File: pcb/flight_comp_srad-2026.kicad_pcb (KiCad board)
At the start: 2 copper layers, 70 x 40 mm, 41 parts, among them J1 503398-1892, J3 USB_B_Micro, U1 IIM-20670, U2 NCP1117-3.3_SOT223, U3 RP2040, U4 ADXL375BCCZ-RL7, U5 MAX-M10M-00B, U6 W25Q128JVS, U7 XBP9B-DMSTB002, Y1 ABM8-272-T3

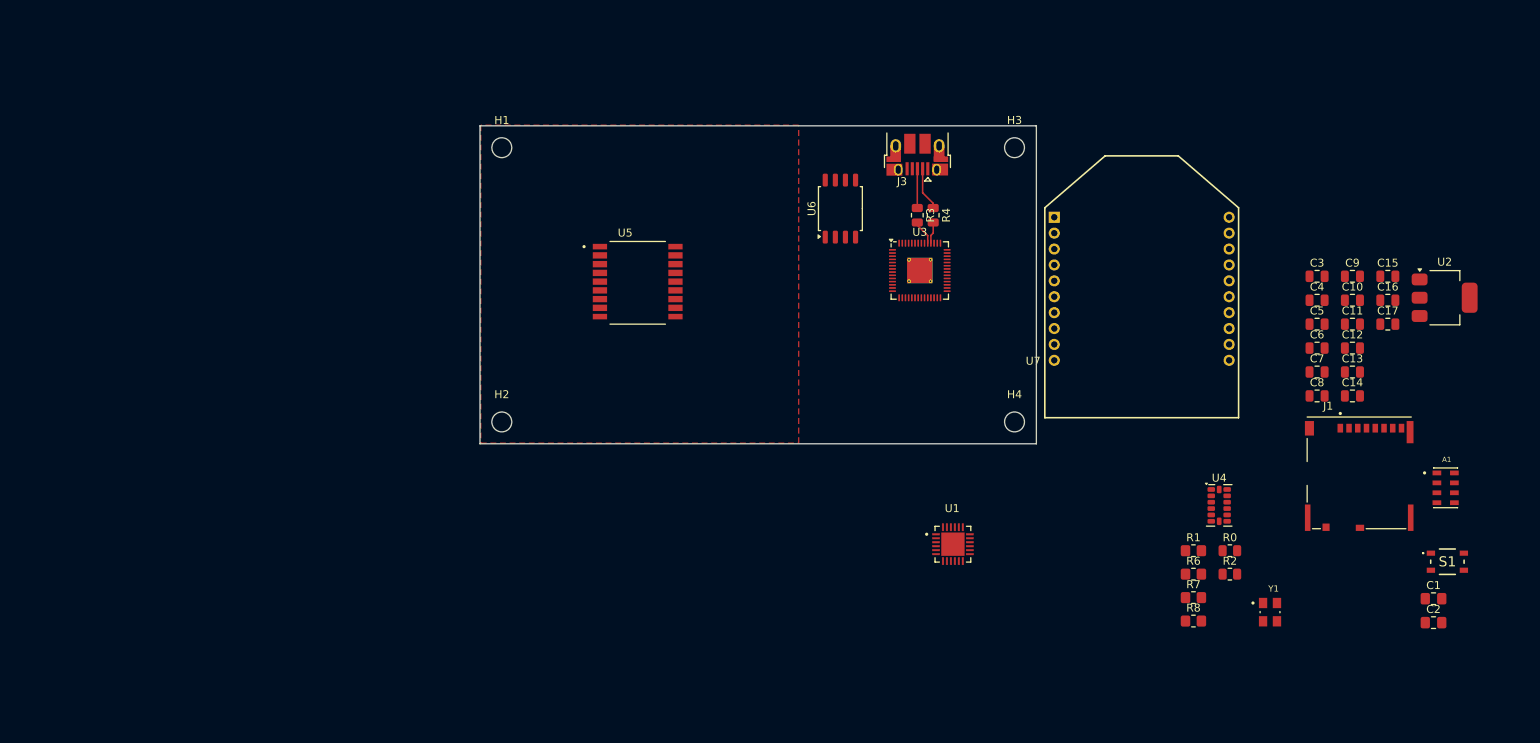
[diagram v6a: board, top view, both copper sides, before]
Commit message: RP2040 listo, faltan sensores y comms
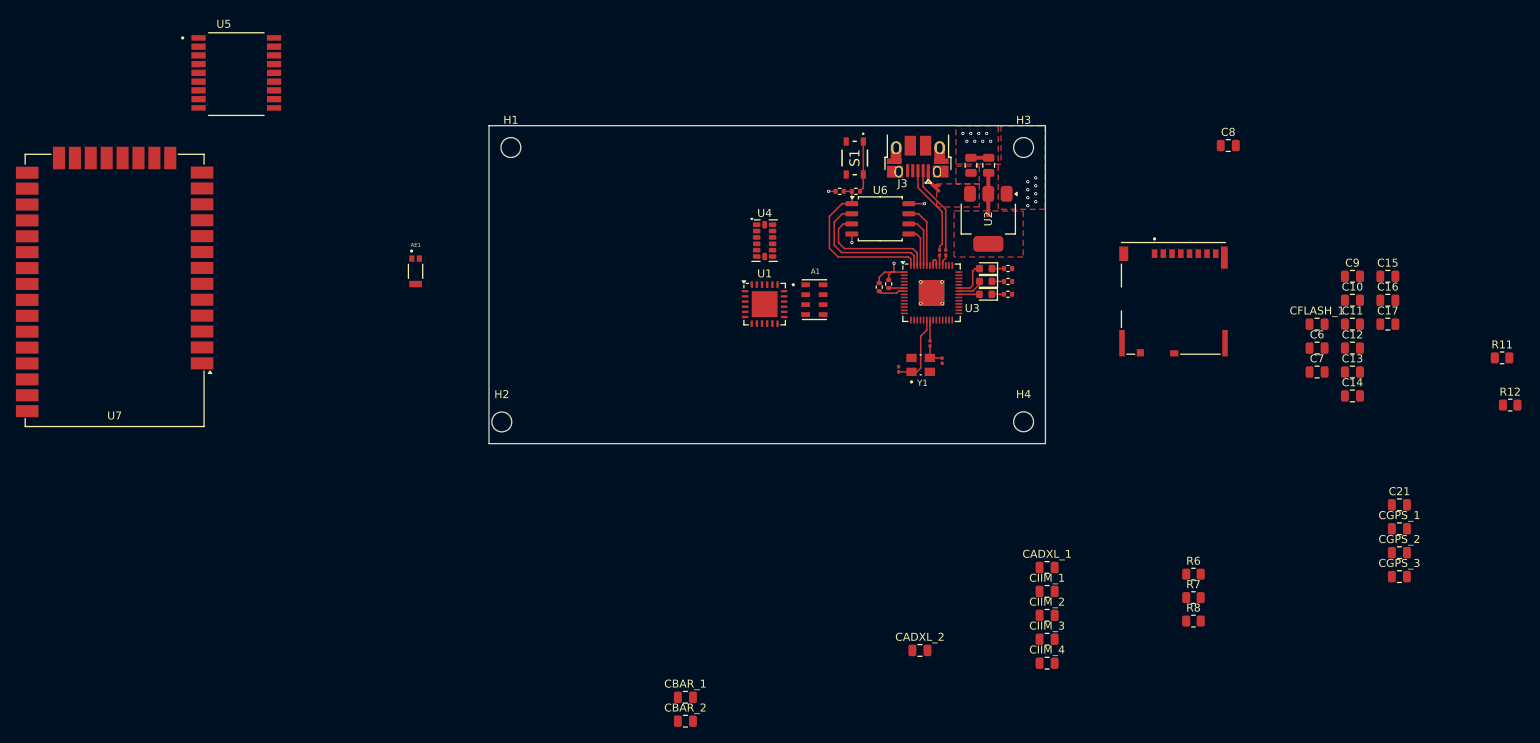
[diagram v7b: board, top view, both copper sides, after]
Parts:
- added AE1: W3011, W3011:XDCR_W3011, F.Cu at (141.9, 78.8)
- added C21: C, Capacitor_SMD:C_0805_2012Metric, F.Cu at (265.7, 108.2)
- added CADXL_1: 100n, Capacitor_SMD:C_0805_2012Metric, F.Cu at (221.3, 116.1)
- added CADXL_2: 1u, Capacitor_SMD:C_0805_2012Metric, F.Cu at (205.3, 126.5)
- added CBAR_1: 100n, Capacitor_SMD:C_0805_2012Metric, F.Cu at (175.8, 132.4)
- added CBAR_2: 100n, Capacitor_SMD:C_0805_2012Metric, F.Cu at (175.8, 135.4)
- added CGPS_1: 100n, Capacitor_SMD:C_0805_2012Metric, F.Cu at (265.7, 111.2)
- added CGPS_2: 100n, Capacitor_SMD:C_0805_2012Metric, F.Cu at (265.7, 114.2)
- added CGPS_3: 100n, Capacitor_SMD:C_0805_2012Metric, F.Cu at (265.7, 117.2)
- added CIIM_1: 100n, Capacitor_SMD:C_0805_2012Metric, F.Cu at (221.3, 119.1)
- added CIIM_2: 100n, Capacitor_SMD:C_0805_2012Metric, F.Cu at (221.3, 122.1)
- added CIIM_3: 100n, Capacitor_SMD:C_0805_2012Metric, F.Cu at (221.3, 125.1)
- added CIIM_4: 100n, Capacitor_SMD:C_0805_2012Metric, F.Cu at (221.3, 128.1)
- added D1: LED, LED_SMD:LED_0603_1608Metric, F.Cu at (213.6, 78.5)
- added D2: LED, LED_SMD:LED_0603_1608Metric, F.Cu at (213.6, 80.1)
- added D3: LED, LED_SMD:LED_0603_1608Metric, F.Cu at (213.6, 81.7)
- added R11: R, Resistor_SMD:R_0805_2012Metric, F.Cu at (278.6, 89.7)
- added R12: R, Resistor_SMD:R_0805_2012Metric, F.Cu at (279.6, 95.6)
- added RI2C_1: 10k, Resistor_SMD:R_0402_1005Metric, F.Cu at (200.2, 80.8)
- added RI2C_2: 10k, Resistor_SMD:R_0402_1005Metric, F.Cu at (201.4, 80.4)
- added RL_1: 1k, Resistor_SMD:R_0402_1005Metric, F.Cu at (216.4, 78.5)
- added RL_2: 1k, Resistor_SMD:R_0402_1005Metric, F.Cu at (216.4, 80.1)
- added RL_3: 1k, Resistor_SMD:R_0402_1005Metric, F.Cu at (216.4, 81.7)
- CX_1: renamed from C1; footprint TCLib:C_0805 -> Capacitor_SMD:C_0201_0603Metric
- CX_2: renamed from C2; footprint TCLib:C_0805 -> Capacitor_SMD:C_0201_0603Metric
- R3, R4: footprint Resistor_SMD:R_0805_2012Metric -> Capacitor_SMD:C_0201_0603Metric
- R6, R7, R8: footprint Resistor_SMD:R_0805_2012Metric_Pad1.20x1.40mm_HandSolder -> Resistor_SMD:R_0805_2012Metric
- RFLASH_1: renamed from R0; footprint Resistor_SMD:R_0805_2012Metric -> Resistor_SMD:R_0402_1005Metric
- RFLASH_2: renamed from R2; footprint Resistor_SMD:R_0805_2012Metric -> Resistor_SMD:R_0402_1005Metric
- RX_1: renamed from R1; footprint Resistor_SMD:R_0805_2012Metric_Pad1.20x1.40mm_HandSolder -> Resistor_SMD:R_0201_0603Metric
- U1: footprint IIM_20670:QFN50P450X450X115-25N -> Package_DFN_QFN:QFN-24-1EP_5x5mm_P0.65mm_EP3.25x3.25mm
- U7: footprint XBEEPRO:XBEEPRO -> RF_Module:Digi_XBee_SMT
- moved U7 129.2 mm to (104.0, 80.5), turned to 180 degrees
- moved S1 90.2 mm to (197.2, 64.5), turned to -90 degrees
- moved A1 82.9 mm to (192.1, 82.4)
- moved CX_1 73.2 mm to (202.7, 91.1), turned to -90 degrees
- moved CX_2 70.1 mm to (208.1, 90.0), turned to 90 degrees
- moved RFLASH_2 67.3 mm to (197.3, 68.7)
- moved RFLASH_1 66.7 mm to (195.3, 68.7)
- moved U4 66.2 mm to (185.8, 74.9)
- moved U2 58.3 mm to (214.0, 72.2), turned to -90 degrees
- moved U5 56.9 mm to (119.3, 53.8)
- moved Y1 53.8 mm to (205.4, 90.6), turned to 90 degrees
- moved CPS_1 45.7 mm to (211.8, 65.5), turned to 90 degrees
- moved CPS_2 44.7 mm to (214.0, 65.5), turned to 90 degrees
- moved RX_1 42.2 mm to (206.6, 87.9), turned to 90 degrees
- moved U1 38.4 mm to (185.8, 82.9)
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- renumbered C5 to CFLASH_1, C3 to CPS_1, C4 to CPS_2
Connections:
- net Net-(U3-USB_DM) renamed /USB_R-
- net Net-(U3-USB_DP) renamed /USB_R+
- A1 pad 1: unconnected-(A1-VDD-Pad1) -> +3V3
- A1 pad 2: unconnected-(A1-PS-Pad2) -> +3V3
- A1 pad 3: unconnected-(A1-GND-Pad3) -> GND
- A1 pad 4: unconnected-(A1-~{CSB}-Pad4) -> +3V3
- A1 pad 5: unconnected-(A1-~{CSB__1}-Pad5) -> +3V3
- A1 pad 7: unconnected-(A1-SDI/SDA-Pad7) -> /ADXL_SDA
- A1 pad 8: unconnected-(A1-SCLK-Pad8) -> /ADXL_SCL
- RFLASH_1 pad 1: +3V3 -> GND
- U1 pad 1: unconnected-(U1-MOSI-Pad1) -> /IIM_MOSI
- U1 pad 10: unconnected-(U1-REGOUT-Pad10) -> Net-(U1-REGOUT)
- U1 pad 11: unconnected-(U1-VDD-Pad11) -> +3V3
- U1 pad 14: unconnected-(U1-GND__5-Pad14) -> GND
- U1 pad 15: unconnected-(U1-GND__6-Pad15) -> GND
- U1 pad 16: unconnected-(U1-GND__7-Pad16) -> GND
- U1 pad 17: unconnected-(U1-GND__8-Pad17) -> GND
- U1 pad 18: unconnected-(U1-~{RESET}-Pad18) -> +3V3
- U1 pad 2: unconnected-(U1-GND-Pad2) -> GND
- U1 pad 20: unconnected-(U1-VPP-Pad20) -> +3V3
- U1 pad 22: unconnected-(U1-GND__9-Pad22) -> GND
- U1 pad 23: unconnected-(U1-NCS-Pad23) -> /IIM_CS
- U1 pad 24: unconnected-(U1-SCLK-Pad24) -> /IIM_SCLK
- U1 pad 3: unconnected-(U1-GND__1-Pad3) -> GND
- U1 pad 4: unconnected-(U1-GND__2-Pad4) -> GND
- U1 pad 5: unconnected-(U1-GND__3-Pad5) -> GND
- U1 pad 7: unconnected-(U1-GND__4-Pad7) -> GND
- U1 pad 8: unconnected-(U1-VDDIO-Pad8) -> +3V3
- U1 pad 9: unconnected-(U1-MISO-Pad9) -> /IIM_MISO
- U3 pad 1: +3V3 -> GND
- U3 pad 35: unconnected-(U3-GPIO23-Pad35) -> /LED_3
- U3 pad 36: unconnected-(U3-GPIO24-Pad36) -> /LED_2
- U3 pad 37: unconnected-(U3-GPIO25-Pad37) -> /LED_1
- U3 pad 6: unconnected-(U3-GPIO4-Pad6) -> /ADXL_SDA
- U3 pad 7: unconnected-(U3-GPIO5-Pad7) -> /ADXL_SCL
- U4 pad 1: unconnected-(U4-VDDI/O-Pad1) -> +3V3
- U4 pad 12: unconnected-(U4-SDO/ALTADDRESS-Pad12) -> GND
- U4 pad 13: unconnected-(U4-SDA/SDI/SDIO-Pad13) -> /ADXL_SDA
- U4 pad 14: unconnected-(U4-SCL/SCLK-Pad14) -> /ADXL_SCL
- U4 pad 2: unconnected-(U4-GND-Pad2) -> GND
- U4 pad 4: unconnected-(U4-GND-Pad4) -> GND
- U4 pad 5: unconnected-(U4-GND-Pad5) -> GND
- U4 pad 6: unconnected-(U4-VS-Pad6) -> +3V3
- U4 pad 7: unconnected-(U4-*CS-Pad7) -> +3V3
- U5 pad 1: unconnected-(U5-GND-Pad1) -> GND
- U5 pad 10: unconnected-(U5-GND__1-Pad10) -> GND
- U5 pad 11: unconnected-(U5-RF_IN-Pad11) -> Net-(U5-RF_IN)
- U5 pad 12: unconnected-(U5-GND__2-Pad12) -> GND
- U5 pad 16: unconnected-(U5-SDA-Pad16) -> /ADXL_SDA
- U5 pad 17: unconnected-(U5-SCL-Pad17) -> /ADXL_SCL
- U5 pad 6: unconnected-(U5-V_BCKP-Pad6) -> +3V3
- U5 pad 7: unconnected-(U5-V_IO-Pad7) -> +3V3
- U5 pad 8: unconnected-(U5-VCC-Pad8) -> +3V3
- U6 pad 8: +3V3 -> GND
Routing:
- net /QSPI_SS: track 0.00 -> 21.7 mm
- net /QSPI_SD1: track 0.00 -> 17.4 mm
- net /QSPI_SD2: track 0.00 -> 15.7 mm
- net GND: track 0.00 -> 13.0 mm, vias 0 -> 20
- net /XIN: track 0.00 -> 9.33 mm
- net /QSPI_SD3: track 0.00 -> 8.15 mm
- net +3V3: track 0.00 -> 7.04 mm
- net /QSPI_SCLK: track 0.00 -> 6.61 mm
- net /USB_D+: track 4.95 -> 11.4 mm
- net /~{USB_BOOT}: track 0.00 -> 6.44 mm
- net /USB_D-: track 5.49 -> 11.2 mm
- net /QSPI_SD0: track 0.00 -> 5.13 mm
- net /LED_1: track 0.00 -> 4.64 mm
- net VBUS: track 0.00 -> 3.85 mm
- net /ADXL_SCL: track 0.00 -> 3.35 mm
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- added copper zone on F.Cu, net +3V3
- added copper zone on In1.Cu, net +3V3
- added copper zone on In2.Cu, net GND
- added copper zone on F.Cu, net VBUS
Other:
- copper layers 2 -> 4

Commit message: cosas del xbee
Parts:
- added CXB_1: C, TCLib:C_0805, F.Cu at (159.0, 95.5)
- added CXB_2: C, TCLib:C_0805, F.Cu at (159.0, 98.5)
- U7: footprint RF_Module:Digi_XBee_SMT -> SRAD_fligh_comp2026:XBEEPRO
- moved U7 57.2 mm to (161.2, 81.2), turned to 90 degrees
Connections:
- RFLASH_1 pad 1: GND -> +3V3
- RI2C_1 pad 2: GND -> +3V3
- RI2C_2 pad 2: GND -> +3V3
- U3 pad 1: GND -> +3V3
- U6 pad 8: GND -> +3V3
- U7 pad 1: unconnected-(U7-VCC-Pad1) -> +3V3
- U7 pad 10: unconnected-(U7-GND-Pad10) -> GND
- U7 pad 2: unconnected-(U7-DOUT/DIO13-Pad2) -> /UART_Rx
- U7 pad 3: unconnected-(U7-DIN/NCONFIG/DIO14-Pad3) -> /UART_Tx
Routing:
- net +3V3: track 7.04 -> 16.7 mm, vias 0 -> 3
- net GND: track 13.0 -> 3.32 mm, vias 20 -> 17
